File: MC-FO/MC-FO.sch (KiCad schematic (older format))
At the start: 17 parts, among them J1 86094327313755E1LF, U161 IFD97, U163 74LVC1G32SE-7, U164 74LVC1G0832DBVT

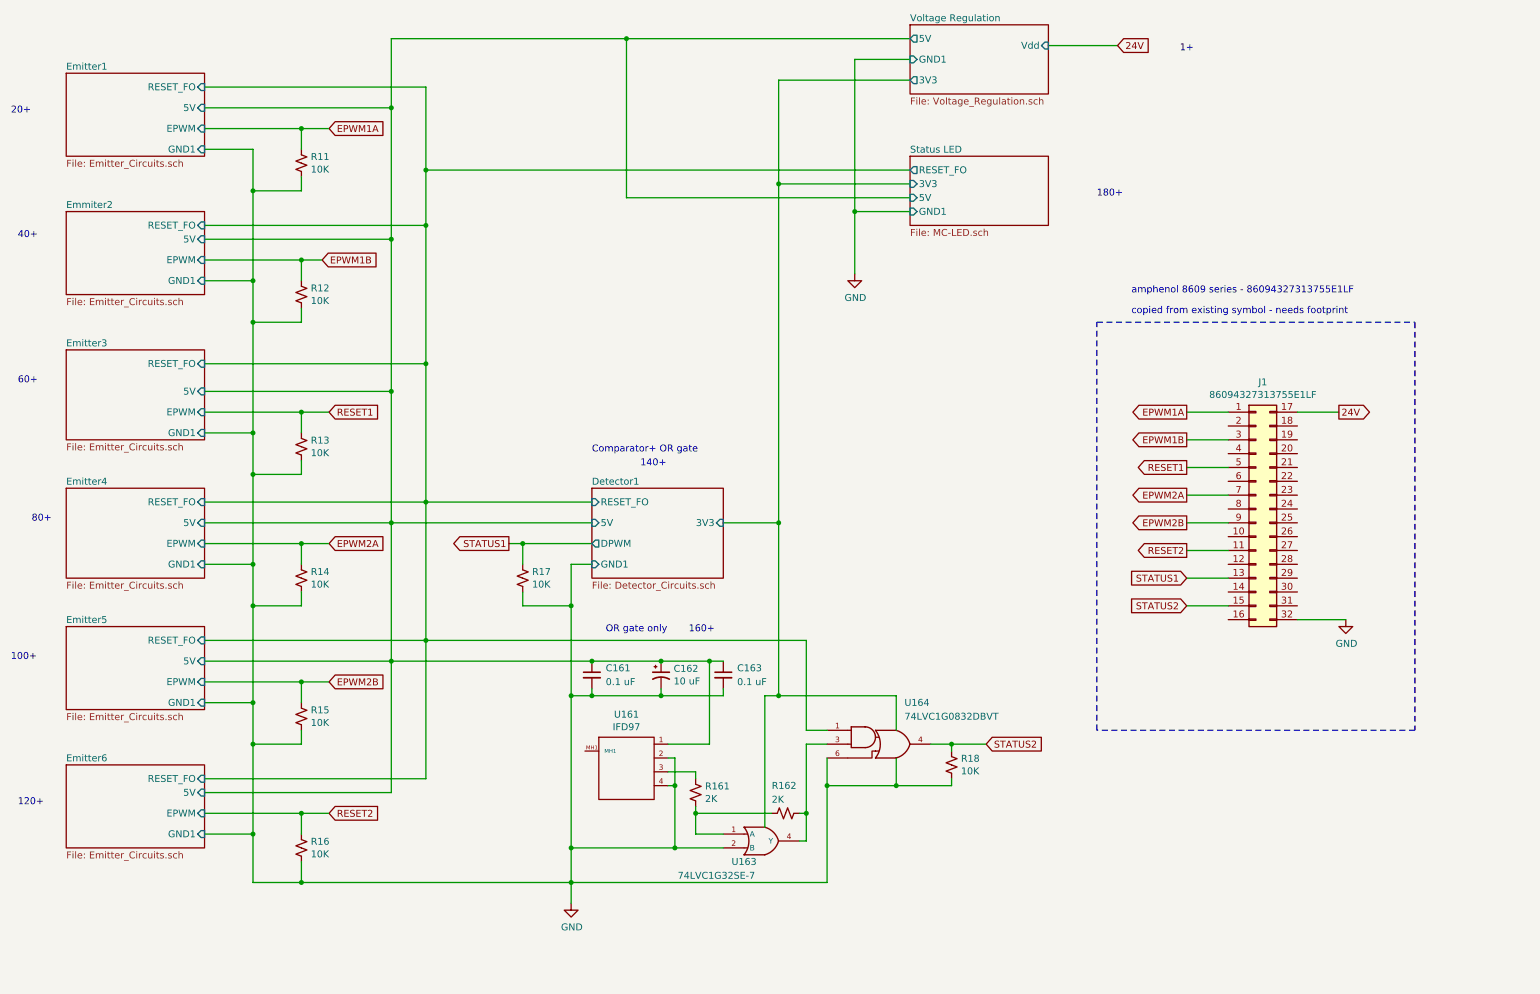
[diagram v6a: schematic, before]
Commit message: changed status1 to output of detector
reassigned footprint of 550 LED
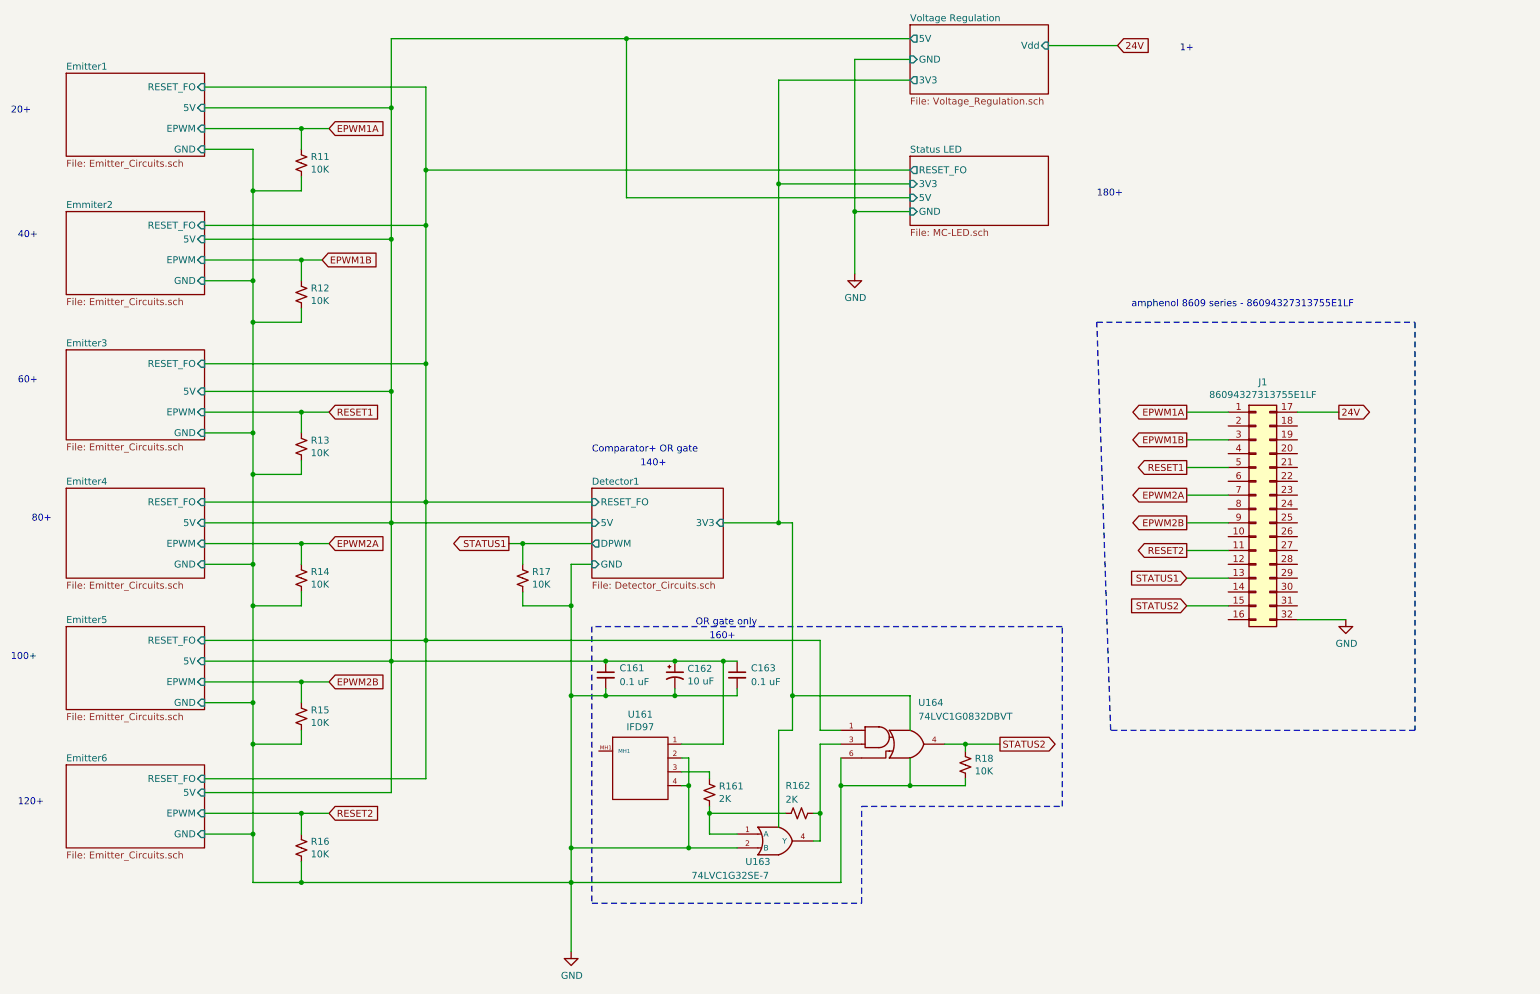
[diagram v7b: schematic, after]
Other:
- note removed: "copied from existing symbol - needs footprint\n"
- moved on the sheet: C161, C162, C163, R161, R162, R18, U161, U163, U164
